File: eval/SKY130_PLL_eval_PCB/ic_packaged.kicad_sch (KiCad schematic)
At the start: 26 parts, among them J3 Conn_02x07_Odd_Even, J5 Conn_02x07_Odd_Even, J6 Conn_02x06_Odd_Even, U2 Caravel_QFN

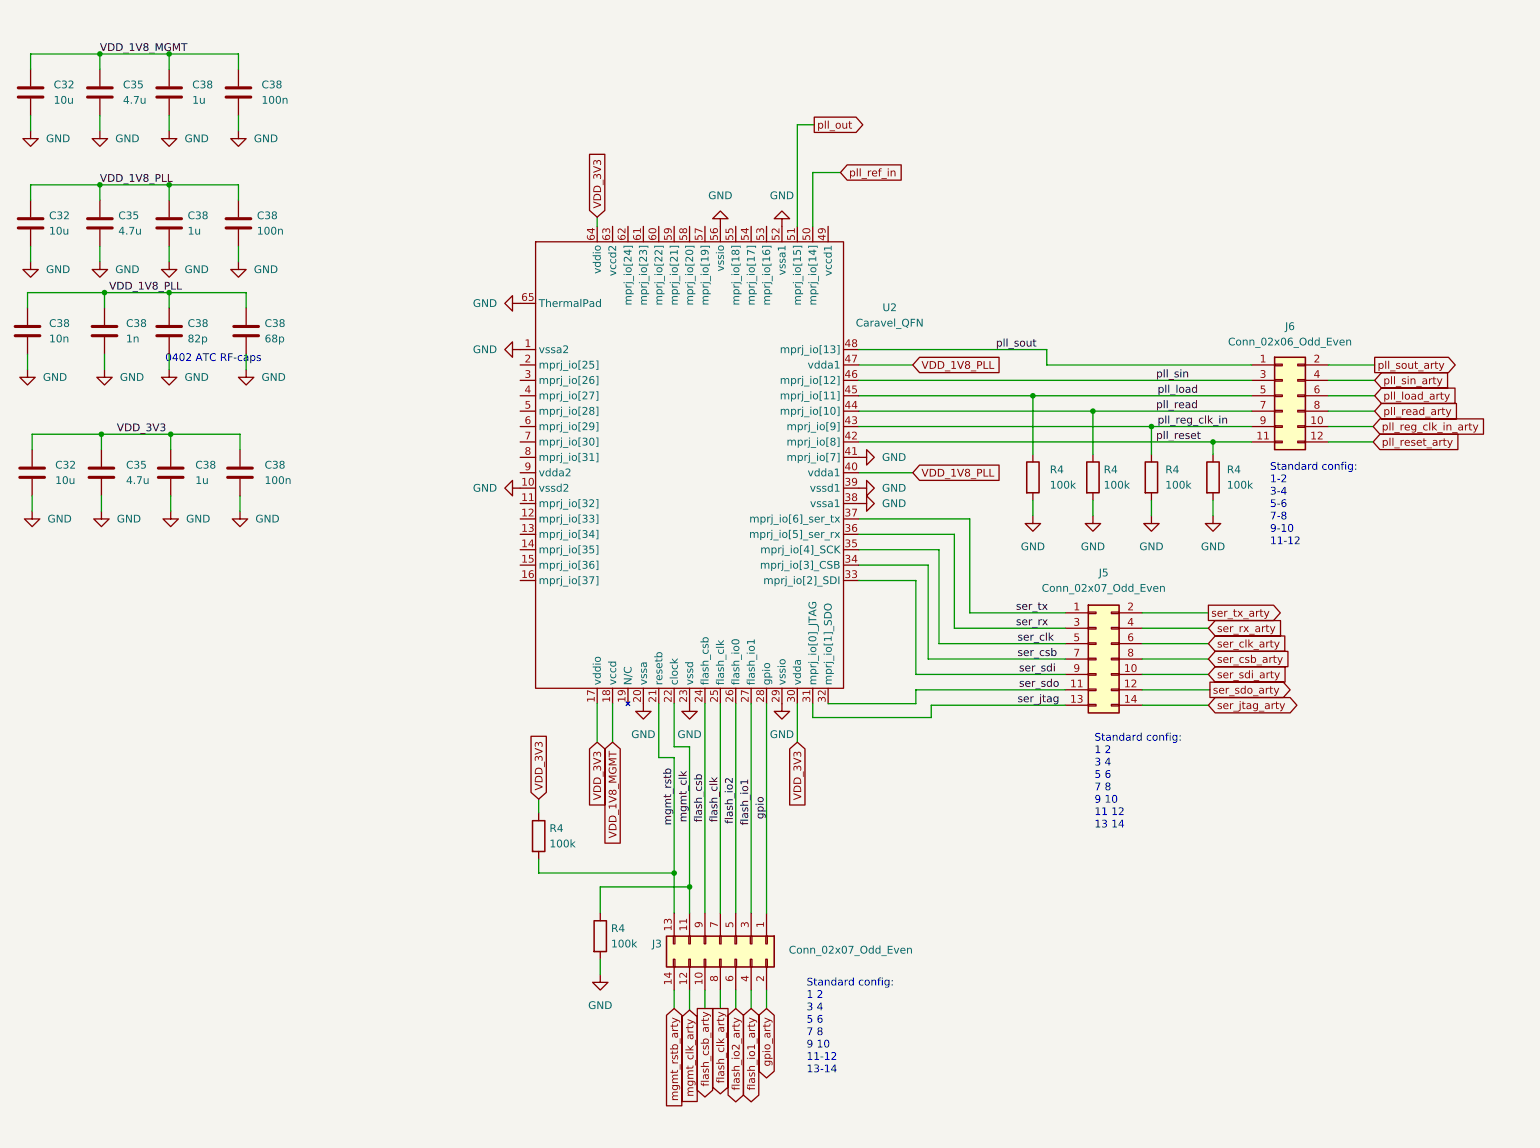
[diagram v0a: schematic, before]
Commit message: eval pcb added
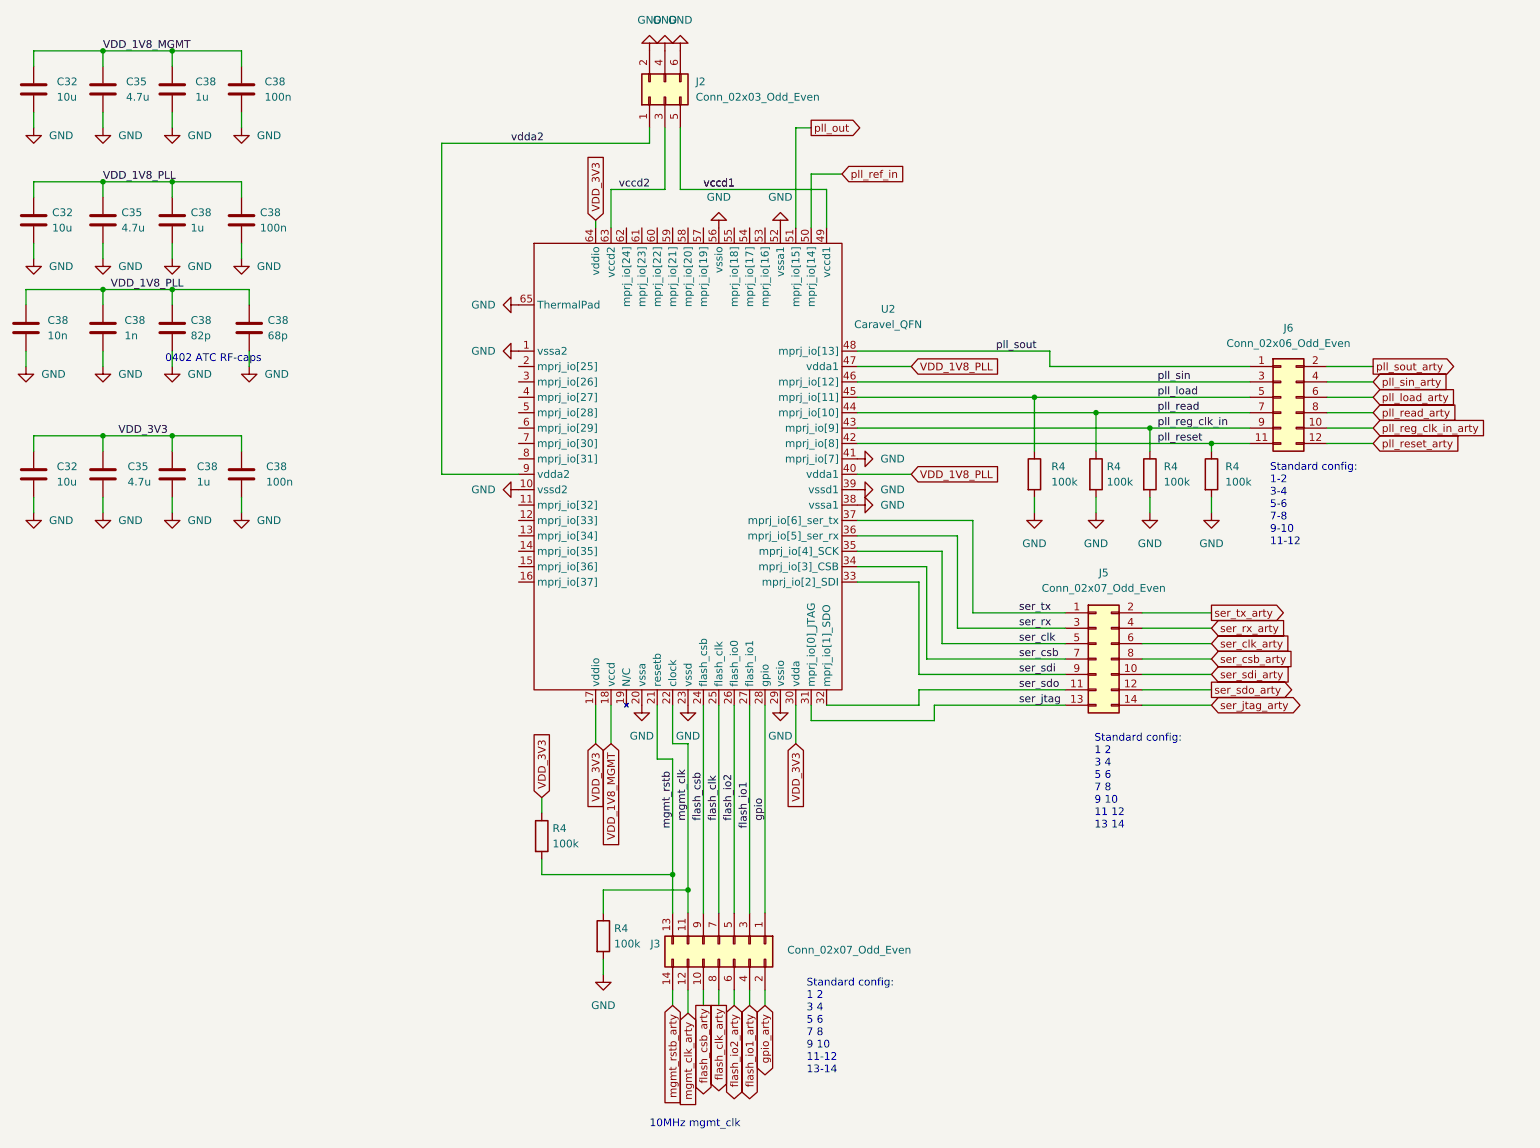
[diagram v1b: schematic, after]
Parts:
- added J2: Conn_02x03_Odd_Even, Connector_PinHeader_2.54mm:PinHeader_2x03_P2.54mm_Vertical_SMD, symbol Connector_Generic:Conn_02x03_Odd_Even
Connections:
- net GND: now also J2.2 (Pin_2), J2.4 (Pin_4), J2.6 (Pin_6)
- net vccd1: now reaches U2.49 (vccd1)
- net vccd1: now also J2.5 (Pin_5)
- net vccd2: now reaches U2.63 (vccd2)
- net vccd2: now also J2.3 (Pin_3)
- net vdda2: now reaches U2.9 (vdda2)
- net vdda2: now also J2.1 (Pin_1)
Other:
- note added: "10MHz mgmt_clk"
- moved on the sheet: C32, C35, C38, R4
